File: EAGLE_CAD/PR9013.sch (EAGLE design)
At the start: 54 parts, among them J1 M3_SCREW_POST, Y1 32.768kHz

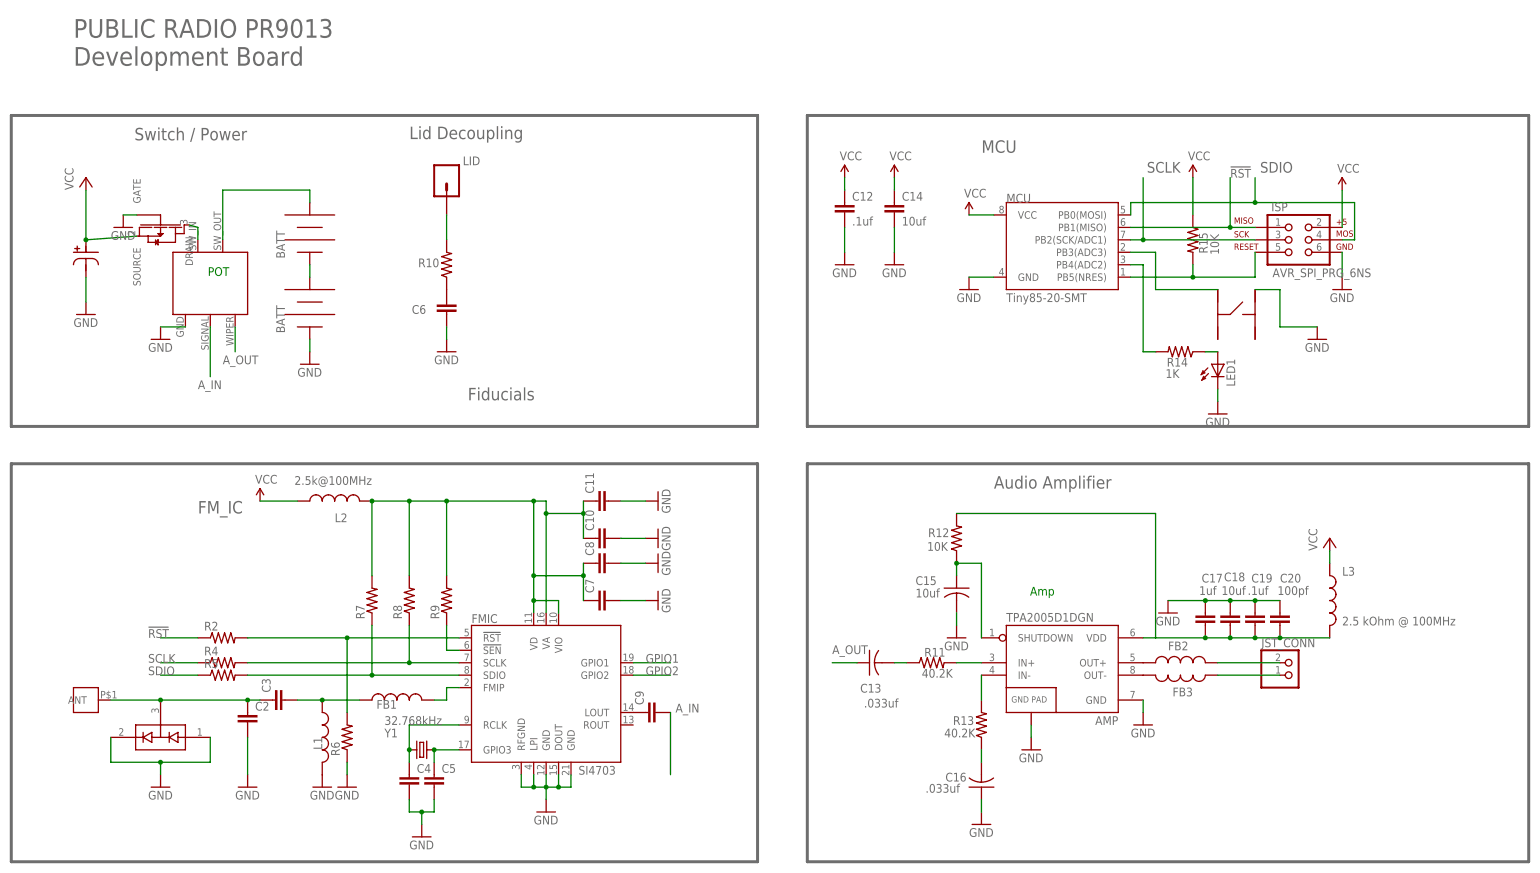
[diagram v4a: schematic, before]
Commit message: Updated SCH and Layout
-Test Points Added
To do:
     o double check locations for errors / conflicts
     o check pad size 1.4 mm big enough?, to big?
-Flattened PCB for alignment
-Changed Xtal package
-Updated PR_Parts_Lib
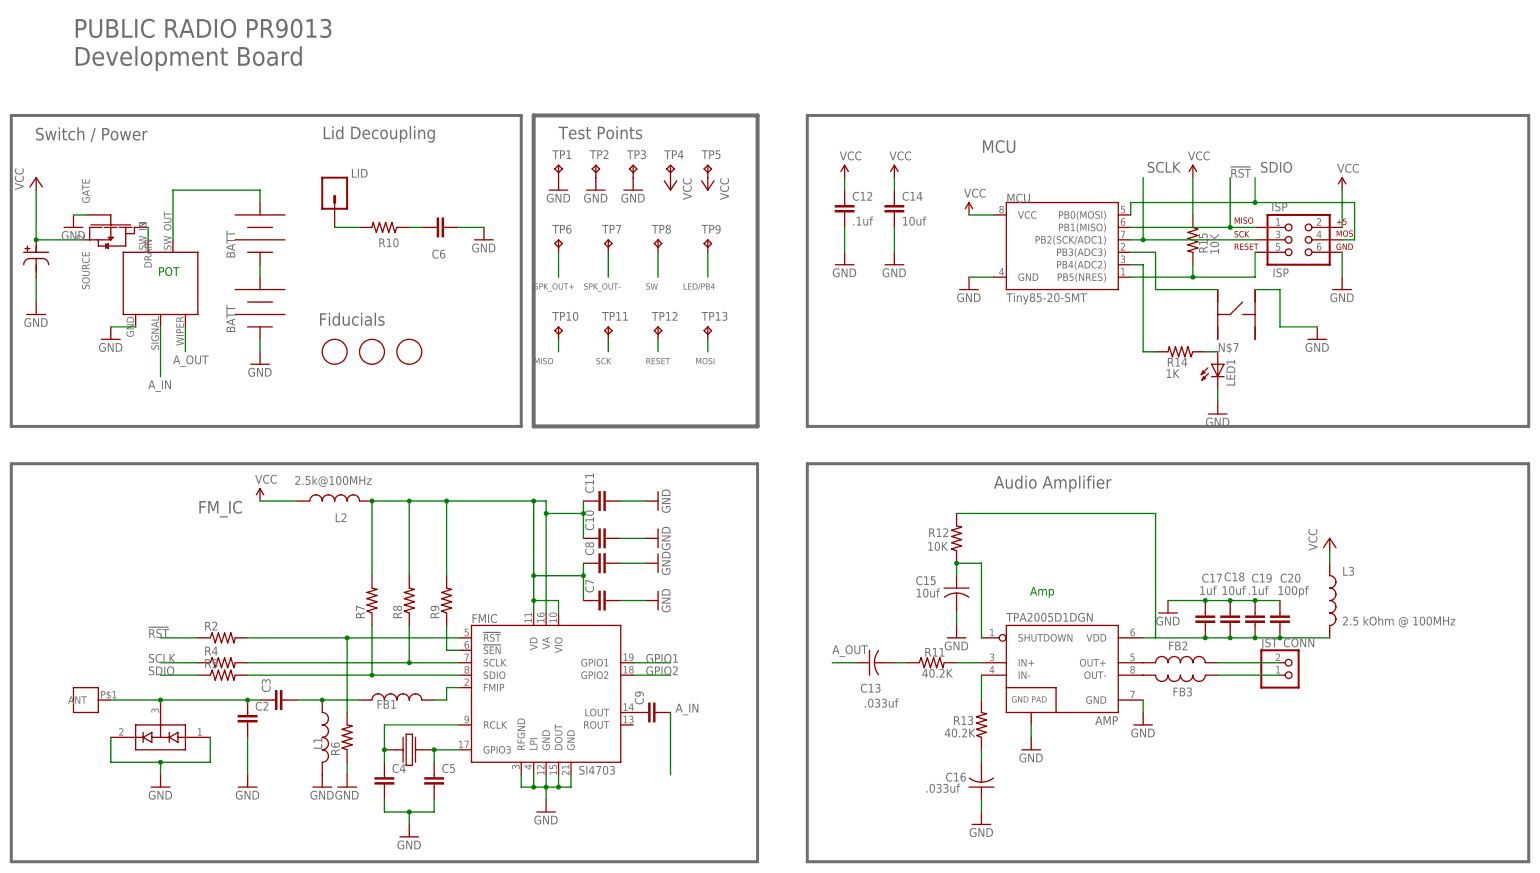
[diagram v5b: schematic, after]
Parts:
- removed Y1: 32.768kHz, SparkFun:CRYSTAL32-SMD
- added TP1, TP10, TP11, TP12, TP13, TP2, TP3, TP4, TP5, TP6, TP7, TP8, TP9: TPTP14R, testpad:TPTP14R
- added U$3, U$4, U$5: FIDUCIAL, adafruit:FIDUCIAL
- added U$6: ABS25XTAL, PR_Parts_Library:ABS25XTAL
- ISP: value AVR_SPI_PRG_6NS -> ISP
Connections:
- removed net N$11: MCU.PB3(ADC3), U$1.P$3
- removed net N$12: MCU.PB4(ADC2), R14.2
- removed net N$22: FB3.1, JST_CONN.2
- removed net N$9: FB2.2, JST_CONN.1
- removed net PB5: ISP.5, MCU.PB5(NRES), R15.2
- new net LED/PB4: MCU.PB4(ADC2), R14.2, TP9.TP
- new net RESET: ISP.5, MCU.PB5(NRES), R15.2, TP12.TP
- new net SPK_OUT+: FB2.2, JST_CONN.1, TP6.TP
- new net SPK_OUT-: FB3.1, JST_CONN.2, TP7.TP
- new net SW: MCU.PB3(ADC3), TP8.TP, U$1.P$3
- net !RST: now also TP10.TP
- net GND: now also TP1.TP, TP2.TP, TP3.TP
- net N$1: now also U$6.P$4; no longer Y1.2
- net N$2: now also U$6.P$1; no longer Y1.1
- net SCLK: now also TP11.TP
- net SDIO: now also TP13.TP
- net VCC: now also TP4.TP, TP5.TP
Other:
- note added: "MISO"
- note added: "MOSI"
- note added: "RESET"
- note added: "SCK"
- note added: "Test Points"
- moved on the sheet: C4, C6, LID, R10

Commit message: layout & package changes
updated a bunch (not all) packages to 0402. crammed everything in more
compactly throughout.

there’s still some sketchy stuff here but it’s not all bad :)
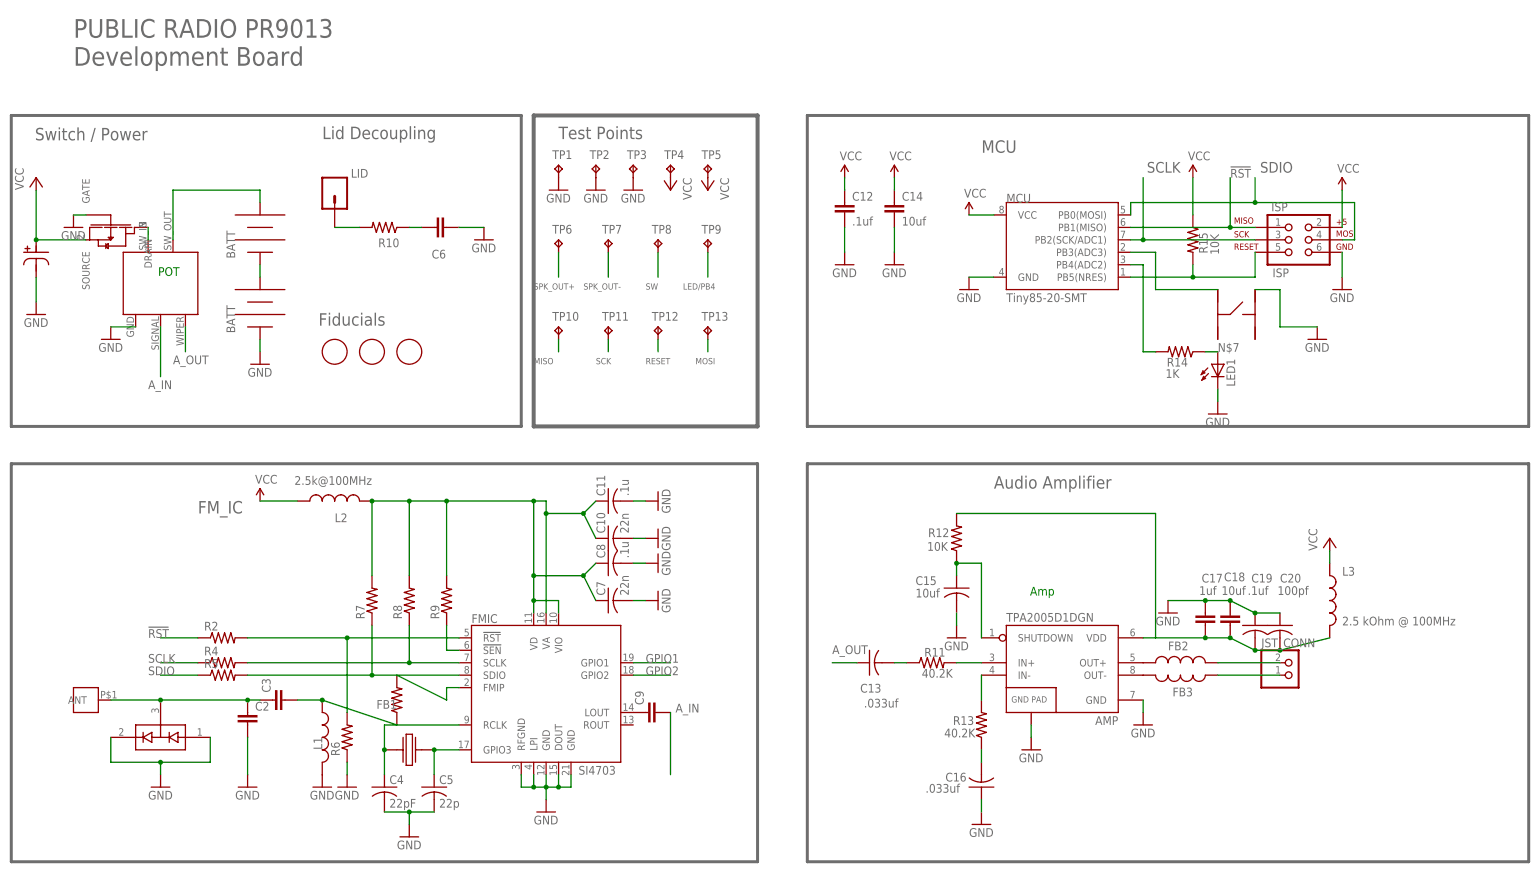
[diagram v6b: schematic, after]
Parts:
- C10, C7: value (none) -> 22n; device SparkFun-Passives:CAP0603-CAP -> resistor:C-USC0402
- C11, C8: value (none) -> .1u; device SparkFun-Passives:CAP0603-CAP -> resistor:C-USC0402
- C13, C16: device resistor:C-USC0603 -> resistor:C-USC0402
- C19, C20: device SparkFun-Passives:CAP0805 -> resistor:C-USC0402
- C4: value (none) -> 22pF; device SparkFun-Passives:CAP0603-CAP -> resistor:C-USC0402
- C5: value (none) -> 22p; device SparkFun-Passives:CAP0603-CAP -> resistor:C-USC0402
- FB1: device SparkFun-Passives:INDUCTOR0805 -> resistor:R-US_R0402
- R11, R12, R13, R14, R15: device resistor:R-US_R0603 -> resistor:R-US_R0402
- R2, R4, R5, R6, R7, R8, R9: device SparkFun-Passives:RESISTOR0603-RES -> resistor:R-US_R0402
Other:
- moved on the sheet: C10, C11, C19, C20, C4, C5, C7, C8

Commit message: Updated SCH and Layout
Changed some 0603 to 0402
Changed some 0805 to 0402
Connected a few traces near the amp
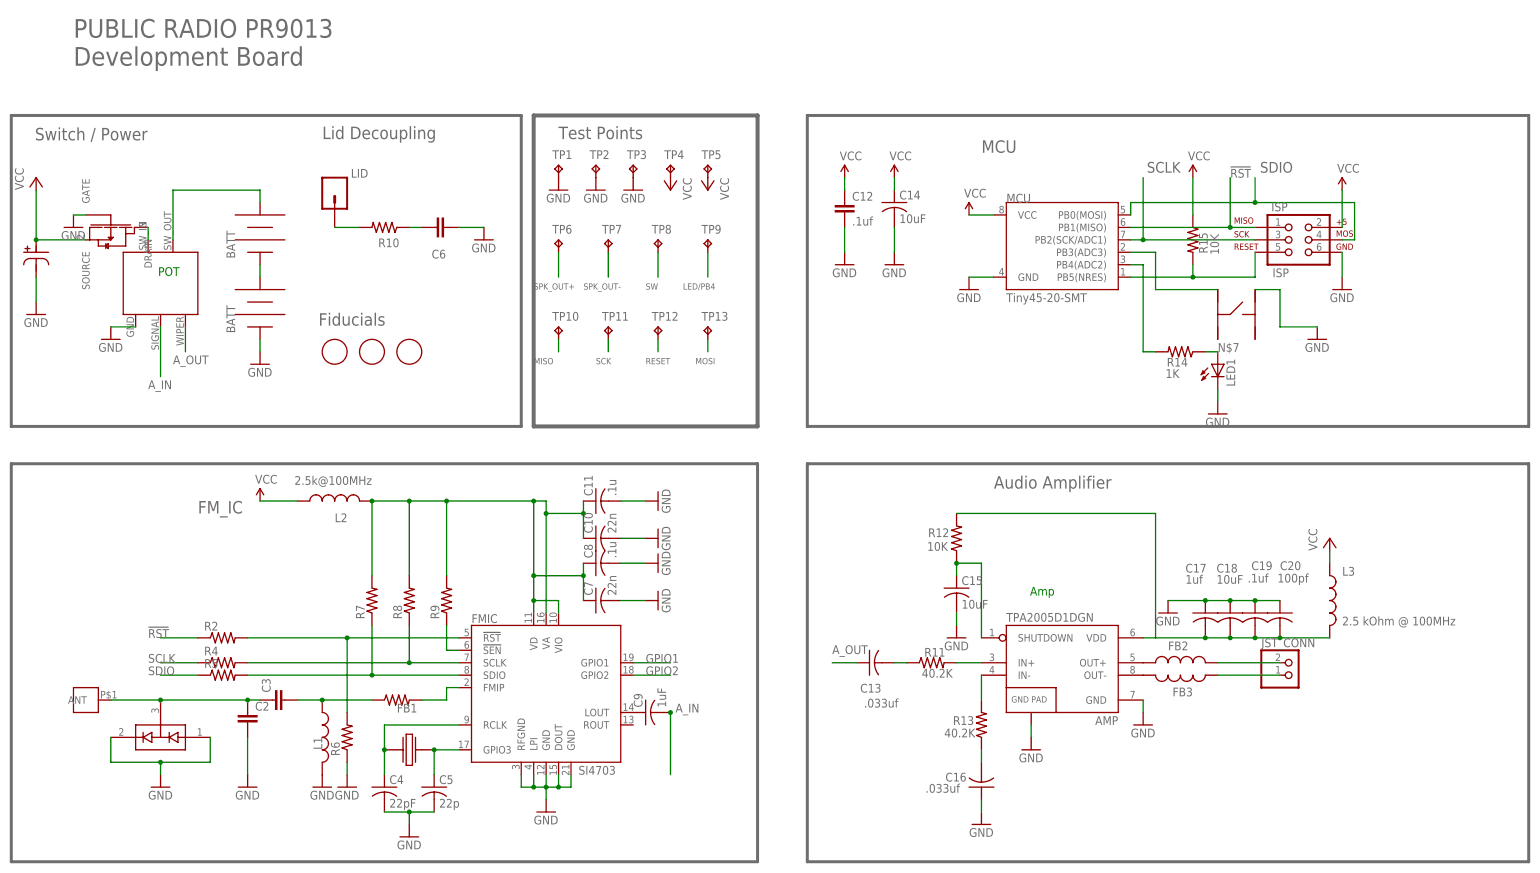
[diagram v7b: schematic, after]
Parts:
- C14, C18: value 10uf -> 10uF; device SparkFun-Passives:CAP0805 -> resistor:C-USC0603
- C15: value 10uf -> 10uF
- C17: device SparkFun-Passives:CAP0805 -> resistor:C-USC0402K
- C9: value (none) -> 1uF; device SparkFun-Passives:CAP0603-CAP -> resistor:C-USC0402K
- MCU: value Tiny85-20-SMT -> Tiny45-20-SMT
- renumbered U$2 to C1
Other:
- moved on the sheet: C10, C11, C19, C20, C7, C8, FB1
